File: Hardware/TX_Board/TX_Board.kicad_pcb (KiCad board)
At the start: 2 copper layers, 216 parts, among them IC1 GP2Y1+, IC10 QPA9122TR7, IC11 MAPS-010164-TR0500, IC12 QPA9122TR7, IC13 MAPS-010164-TR0500, IC14 QPA9122TR7, IC2 GP2Y1+, IC3 GP2Y1+, IC4 LT3041ADE#PBF, IC5 LT3099ADE#PBF, IC6 ADPL40502AUJZ-1.5-R7, IC7 MAPS-010164-TR0500, IC8 QPA9122TR7, IC9 MAPS-010164-TR0500, J1 Conn_Coaxial, J10 MM8030-2610RJ3, J11 MM8030-2610RJ3, J12 MM8030-2610RJ3, J13 MM8030-2610RJ3, J14 MM8030-2610RJ3, J15 Conn_Coaxial, J16 MM8030-2610RJ3, J17 MM8030-2610RJ3, J18 Conn_Coaxial, J19 MM8030-2610RJ3, J2 Conn_01x01_Pin, J20 MM8030-2610RJ3, J21 Conn_Coaxial, J22 MM8030-2610RJ3, J23 MM8030-2610RJ3, J24 Conn_Coaxial, J3 Conn_01x01_Pin, J4 Conn_01x01_Pin, J5 Conn_01x01_Pin, J6 Conn_02x12_Odd_Even, J7 Conn_01x03_Socket, J8 Conn_02x08_Odd_Even, J9 MM8030-2610RJ3, U1 SN74HCT138NSR

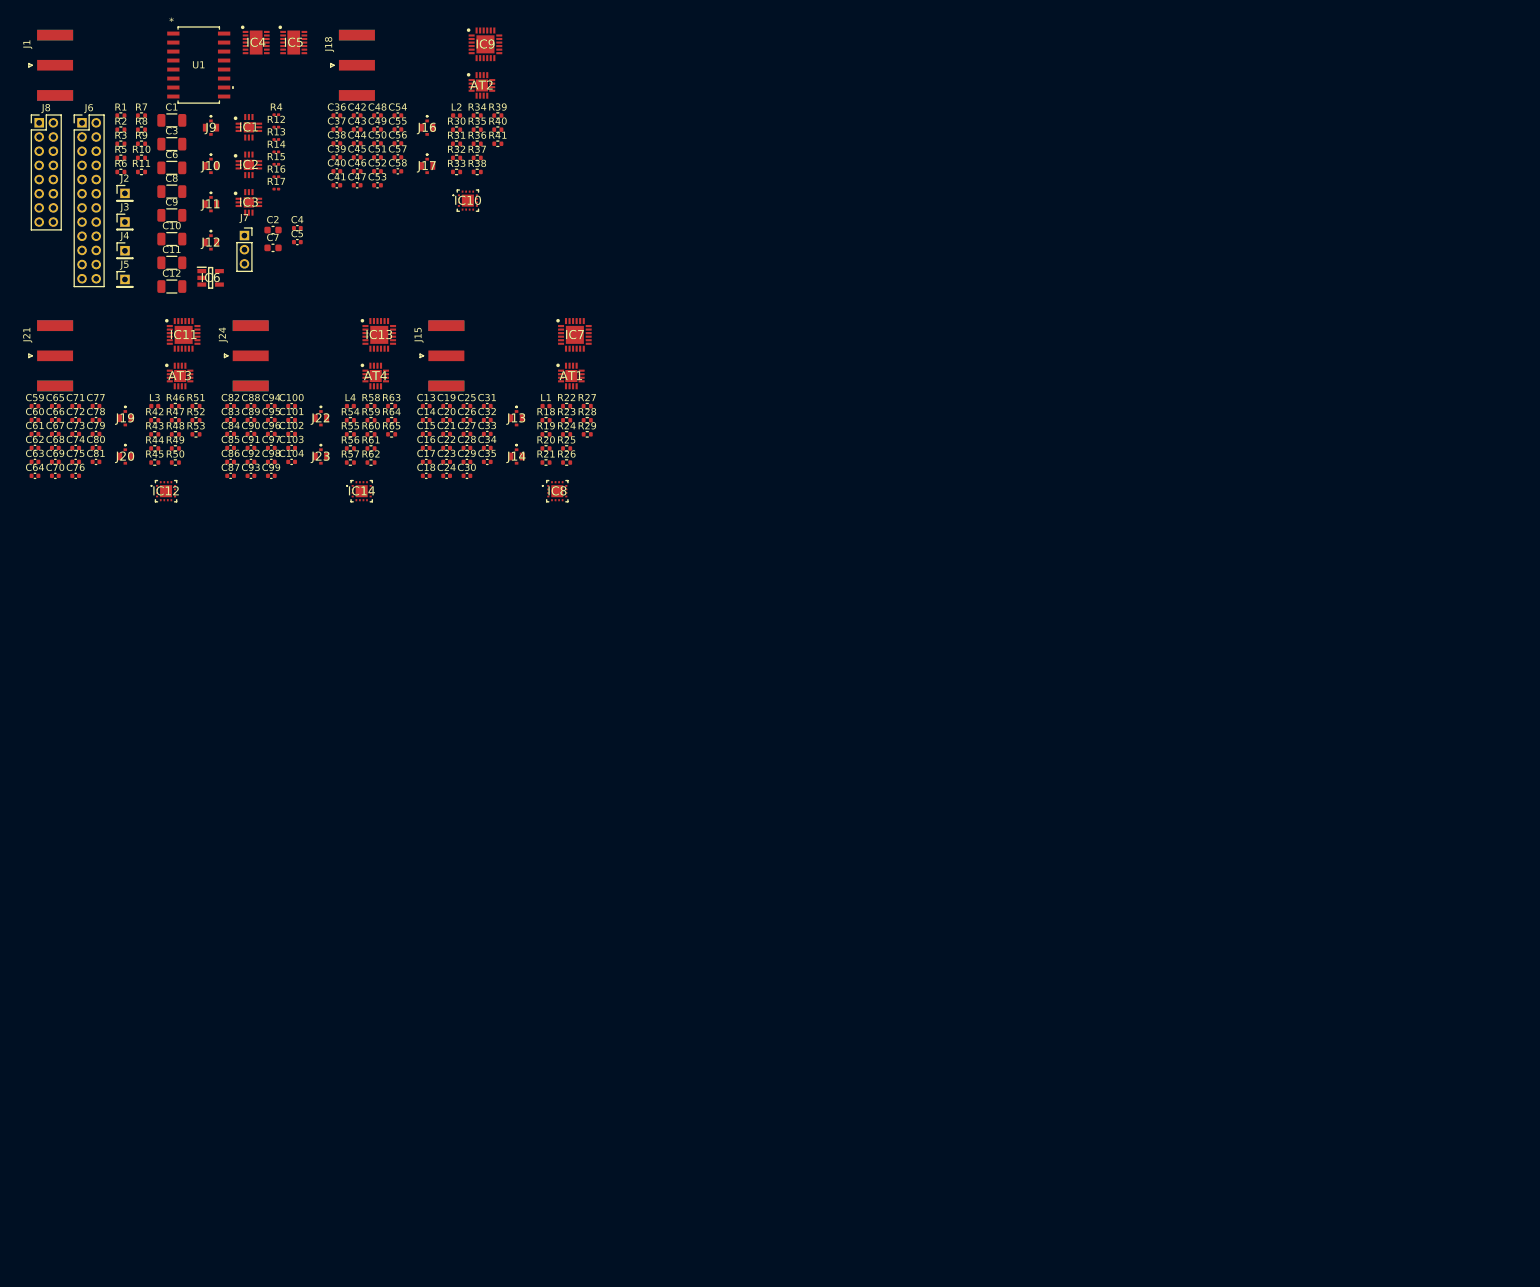
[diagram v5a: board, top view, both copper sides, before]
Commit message: rough layout using replicate plugin
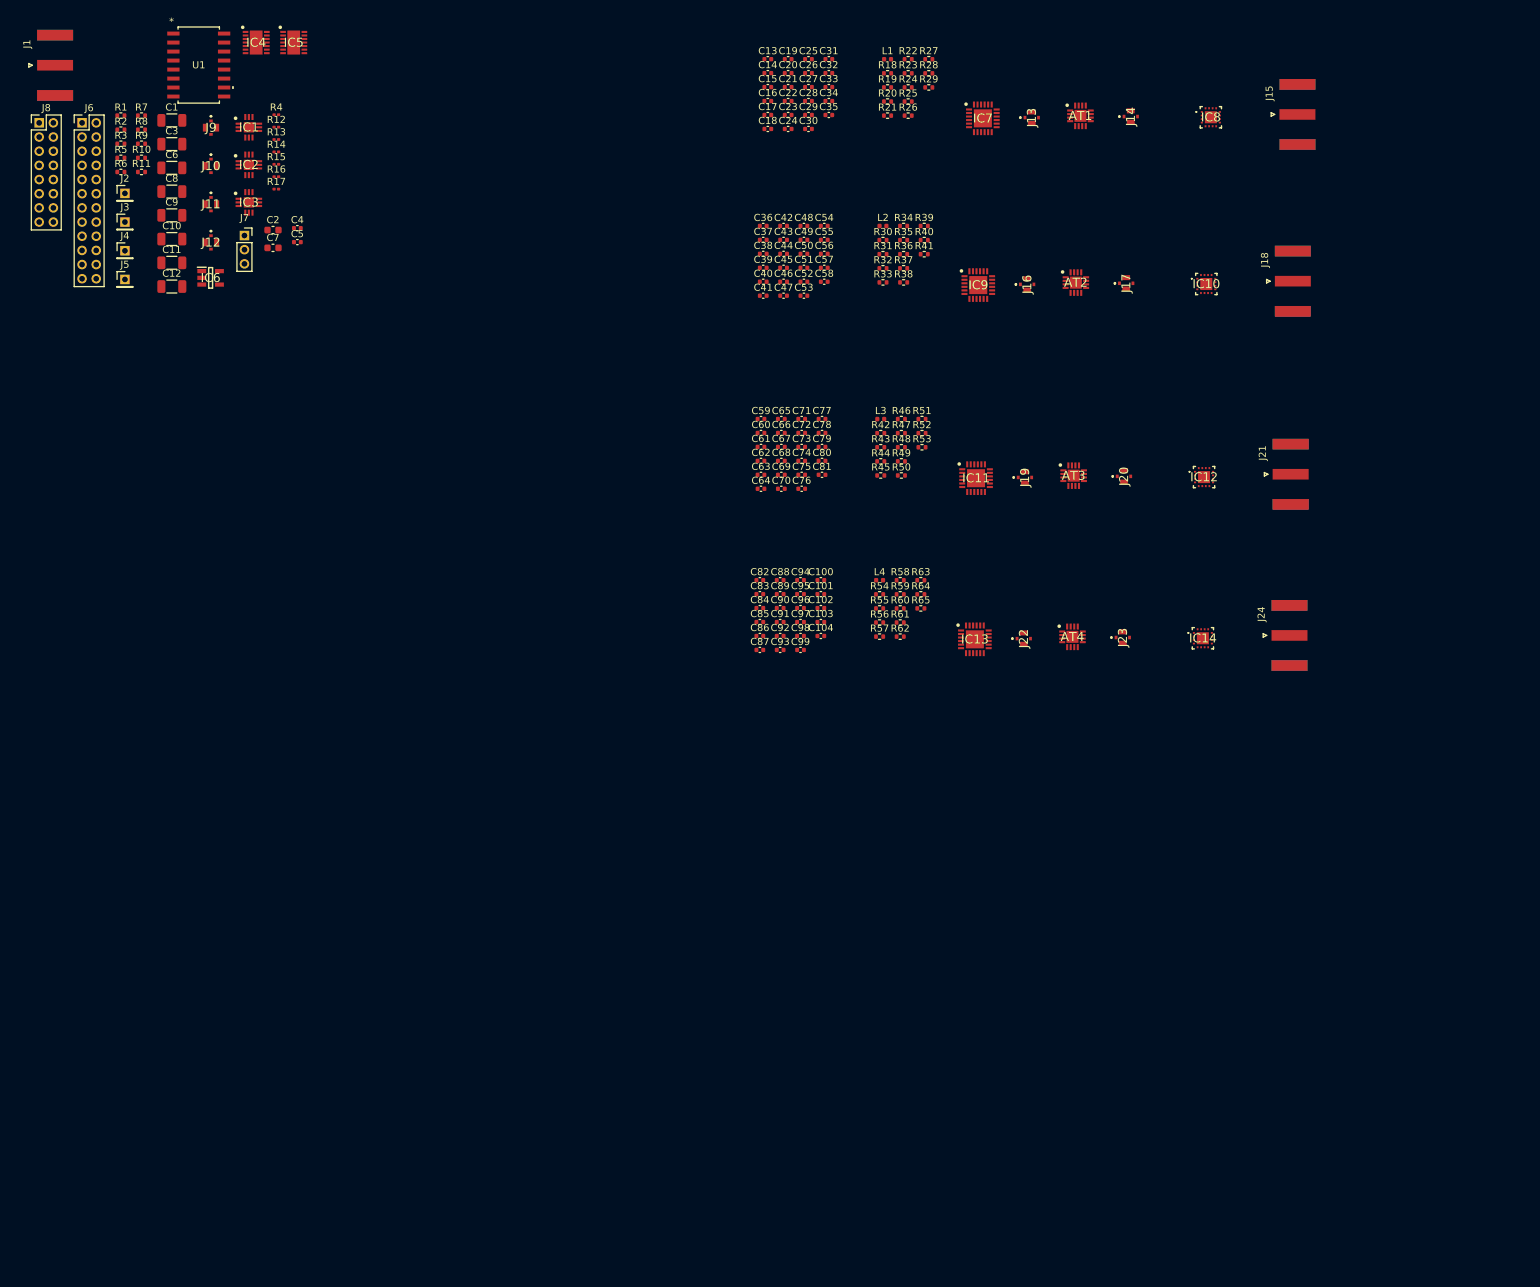
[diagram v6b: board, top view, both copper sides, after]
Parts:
- moved J21 175.2 mm to (205.9, 84.4)
- moved J24 151.8 mm to (205.7, 107.1)
- moved IC12 146.5 mm to (193.7, 84.8)
- moved J20 141.0 mm to (182.4, 84.7), turned to 90 degrees
- moved J18 135.6 mm to (206.2, 57.1)
- moved J19 127.2 mm to (168.4, 84.8), turned to 90 degrees
- moved AT3 126.9 mm to (175.3, 84.6)
- moved J15 124.9 mm to (206.9, 33.6)
- moved IC14 120.5 mm to (193.5, 107.5)
- moved J23 116.0 mm to (182.2, 107.4), turned to 90 degrees
- moved IC11 113.7 mm to (161.5, 84.9)
- moved IC8 106.3 mm to (194.6, 34.0)
- moved AT4 105.0 mm to (175.1, 107.3)
- moved IC10 104.9 mm to (194.0, 57.5)
- moved J22 104.0 mm to (168.2, 107.6), turned to 90 degrees
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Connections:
- R32 pad 2: PS_LE_1 -> PS_LE_2
- R36 pad 2: ATTN_LE_1 -> ATTN_LE_2
- R44 pad 2: PS_LE_1 -> PS_LE_3
- R48 pad 2: ATTN_LE_1 -> ATTN_LE_3
- R56 pad 2: PS_LE_1 -> PS_LE_4
- R60 pad 2: ATTN_LE_1 -> ATTN_LE_4

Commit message: Updated Layout
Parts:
- moved J9 84.2 mm to (137.8, 35.0), turned to 90 degrees
- moved C58 73.1 mm to (213.1, 59.0)
- moved C81 73.1 mm to (212.8, 86.3)
- moved C104 73.1 mm to (212.6, 109.0)
- moved C35 72.4 mm to (213.1, 35.5)
- moved C74 69.1 mm to (205.9, 85.8)
- moved C97 69.1 mm to (205.7, 108.5)
- moved C51 69.1 mm to (206.2, 58.5)
- moved C28 68.4 mm to (206.2, 35.0)
- moved J1 53.4 mm to (32.4, 80.0), turned to 180 degrees
- moved J18 30.4 mm to (236.6, 59.0)
- moved J21 30.4 mm to (236.2, 86.3)
- moved J24 30.4 mm to (236.1, 109.0)
- moved C18 30.0 mm to (102.1, 35.6)
- moved R27 30.0 mm to (124.8, 25.8)
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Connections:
- C28 pad 1: Net-(AT1-RFOUT) -> Net-(J14-OUT)
- C28 pad 2: Net-(J14-IN) -> Net-(IC8-RFIN)
- C51 pad 1: Net-(AT2-RFOUT) -> Net-(J17-OUT)
- C51 pad 2: Net-(J17-IN) -> Net-(IC10-RFIN)
- C74 pad 1: Net-(AT3-RFOUT) -> Net-(J20-OUT)
- C74 pad 2: Net-(J20-IN) -> Net-(IC12-RFIN)
- C97 pad 1: Net-(AT4-RFOUT) -> Net-(J23-OUT)
- C97 pad 2: Net-(J23-IN) -> Net-(IC14-RFIN)
- J14 pad 1: Net-(J14-IN) -> Net-(AT1-RFOUT)
- J14 pad 2: Net-(IC8-RFIN) -> Net-(J14-OUT)
- J17 pad 1: Net-(J17-IN) -> Net-(AT2-RFOUT)
- J17 pad 2: Net-(IC10-RFIN) -> Net-(J17-OUT)
- J20 pad 1: Net-(J20-IN) -> Net-(AT3-RFOUT)
- J20 pad 2: Net-(IC12-RFIN) -> Net-(J20-OUT)
- J23 pad 1: Net-(J23-IN) -> Net-(AT4-RFOUT)
- J23 pad 2: Net-(IC14-RFIN) -> Net-(J23-OUT)
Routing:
- net Net-(J21-In): track 0.00 -> 45.9 mm
- net Net-(J18-In): track 0.00 -> 45.9 mm
- net Net-(J24-In): track 0.00 -> 45.9 mm
- net VCC: track 0.00 -> 30.3 mm
- net Net-(IC9-RF_OUT): track 0.00 -> 23.5 mm
- net Net-(IC13-RF_OUT): track 0.00 -> 23.5 mm
- net Net-(IC11-RF_OUT): track 0.00 -> 23.5 mm
- net Net-(AT4-RFOUT): track 0.00 -> 23.5 mm
- net Net-(AT3-RFOUT): track 0.00 -> 23.5 mm
- net Net-(AT2-RFOUT): track 0.00 -> 23.5 mm
- net Net-(J15-In): track 0.00 -> 23.0 mm
- net Net-(J23-OUT): track 0.00 -> 16.5 mm
- net Net-(J20-OUT): track 0.00 -> 16.5 mm
- net Net-(J17-OUT): track 0.00 -> 16.5 mm
- net Net-(AT4-RFIN): track 0.00 -> 16.0 mm
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
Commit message: More Layout
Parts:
- added C105: 1 uF, Capacitor_SMD:C_0402_1005Metric, F.Cu at (210.1, 38.7)
- added C106: 100 pF, Capacitor_SMD:C_0402_1005Metric, F.Cu at (210.1, 39.7)
- added C107: 1 uF, Capacitor_SMD:C_0402_1005Metric, F.Cu at (210.1, 63.0)
- added C108: 100 pF, Capacitor_SMD:C_0402_1005Metric, F.Cu at (210.1, 64.0)
- added C109: 1 uF, Capacitor_SMD:C_0402_1005Metric, F.Cu at (210.1, 87.2)
- added C110: 100 pF, Capacitor_SMD:C_0402_1005Metric, F.Cu at (210.1, 88.2)
- added C111: 1 uF, Capacitor_SMD:C_0402_1005Metric, F.Cu at (210.1, 111.5)
- added C112: 100 pF, Capacitor_SMD:C_0402_1005Metric, F.Cu at (210.1, 112.5)
- moved J12 105.9 mm to (138.2, 115.3), turned to 90 degrees
- moved C102 105.1 mm to (215.0, 112.0)
- moved C103 105.0 mm to (215.0, 113.0)
- moved C79 104.8 mm to (215.0, 87.7)
- moved C80 104.8 mm to (215.0, 88.7)
- moved C56 104.8 mm to (215.0, 63.5)
- moved C33 104.7 mm to (215.0, 39.2)
- moved C57 104.7 mm to (215.0, 64.5)
- moved C34 104.6 mm to (215.0, 40.2)
- moved C98 104.1 mm to (210.6, 120.5)
- moved C99 104.0 mm to (210.6, 121.5)
- moved C52 103.8 mm to (210.6, 72.0)
- moved C75 103.7 mm to (210.6, 96.2)
- moved C29 103.7 mm to (210.6, 47.7)
- moved C53 103.7 mm to (210.6, 73.0)
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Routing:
- net Net-(J21-In): track 45.9 -> 11.9 mm
- net Net-(J18-In): track 45.9 -> 11.9 mm
- net Net-(J24-In): track 45.9 -> 11.9 mm
- net VCC: track 30.3 -> 48.6 mm
- net Net-(J15-In): track 23.0 -> 11.9 mm
- net Net-(IC9-RF_OUT): track 23.5 -> 12.7 mm
- net Net-(IC13-RF_OUT): track 23.5 -> 12.7 mm
- net Net-(IC11-RF_OUT): track 23.5 -> 12.7 mm
- net Net-(AT4-RFOUT): track 23.5 -> 12.8 mm
- net Net-(AT3-RFOUT): track 23.5 -> 12.8 mm
- net Net-(AT2-RFOUT): track 23.5 -> 12.8 mm
- net Net-(J23-OUT): track 16.5 -> 8.31 mm
- net Net-(J20-OUT): track 16.5 -> 8.31 mm
- net Net-(J17-OUT): track 16.5 -> 8.31 mm
- net Net-(IC1-PORT_2): track 0.00 -> 8.17 mm
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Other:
- board outline added: 148 x 98.8 mm
